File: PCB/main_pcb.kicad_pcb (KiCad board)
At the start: 2 copper layers, 116.9 x 116.9 mm, 40 parts, among them P1 SEN, P2 SRV, P3 PWR, P4 LED, P5 M1, P6 M2, P7 CONN_02X03, P8 CONN_02X03, P9 Range, Q1 5LN01SP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

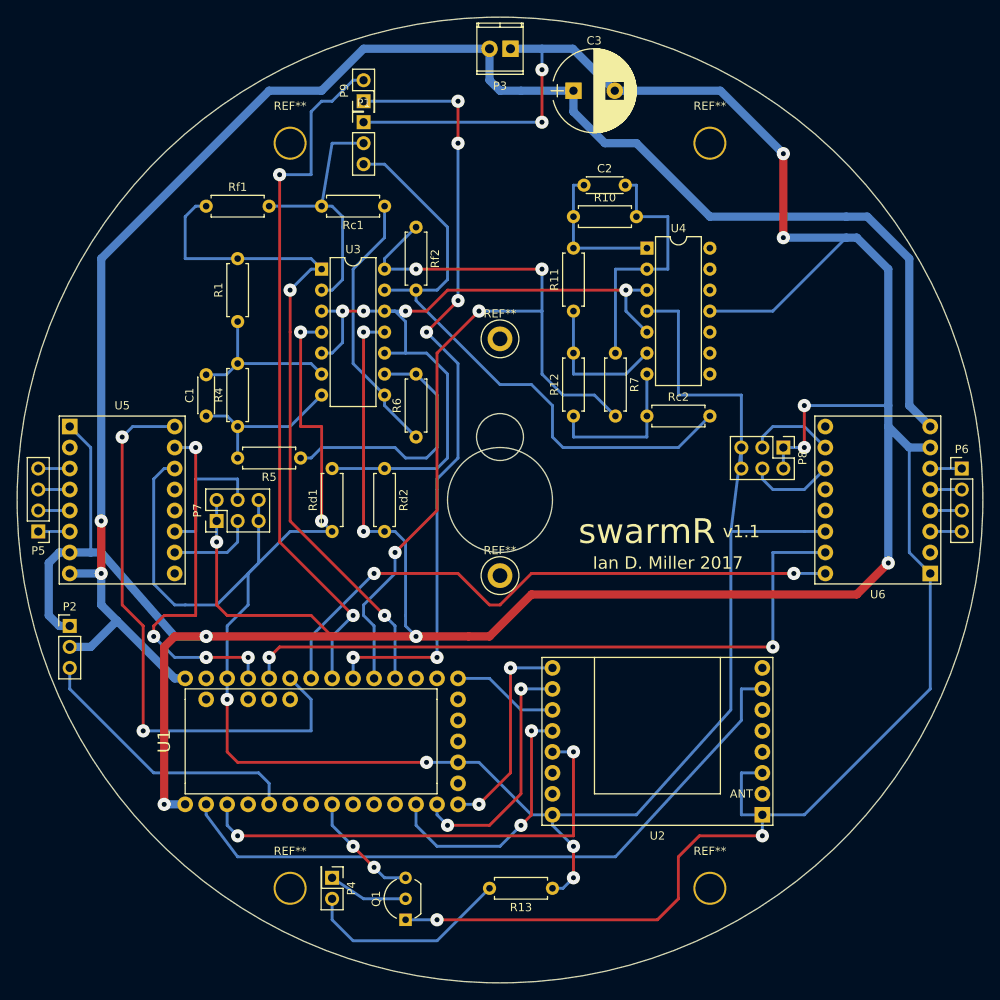
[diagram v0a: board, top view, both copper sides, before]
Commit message: Added copper pours
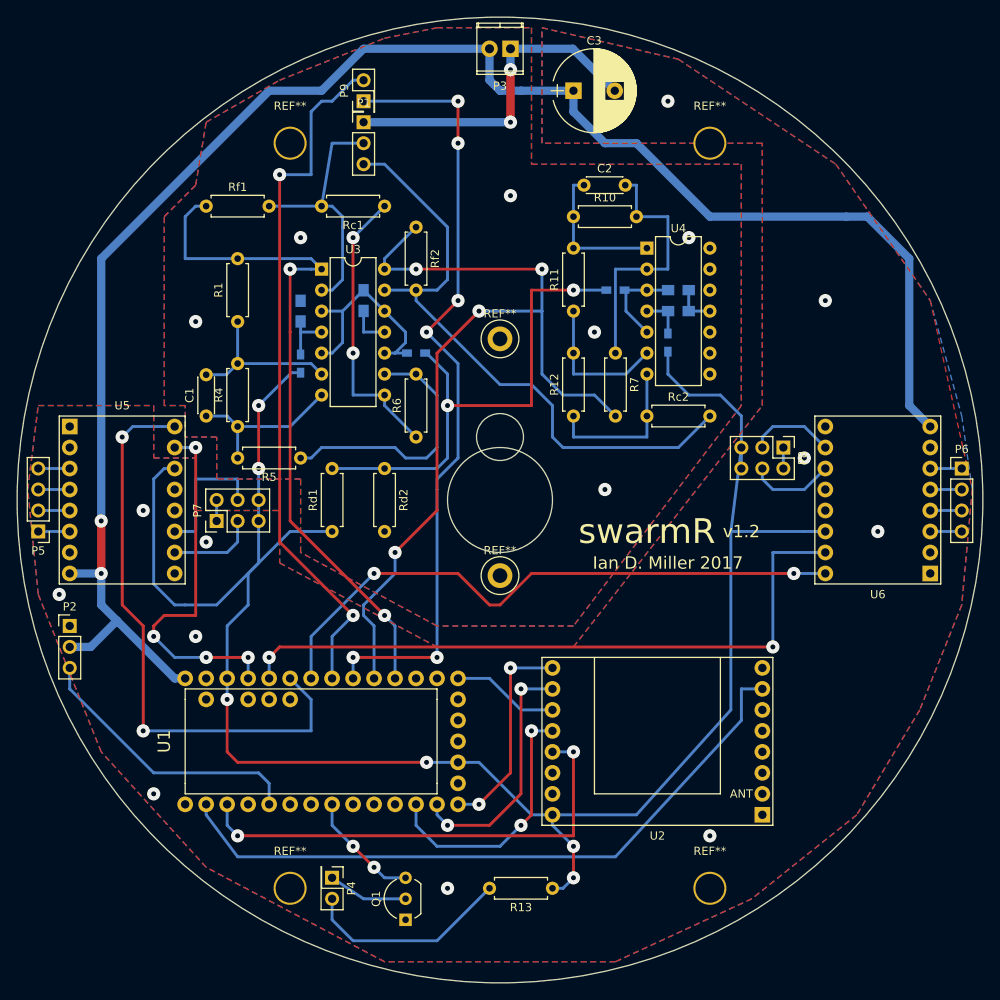
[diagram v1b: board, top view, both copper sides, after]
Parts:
- added C4: 10u, Capacitors_SMD:C_0805_HandSoldering, B.Cu at (114.3, 72.4)
- added C5: 10u, Capacitors_SMD:C_0805_HandSoldering, B.Cu at (121.9, 71.1)
- added C6: 10u, Capacitors_SMD:C_0805_HandSoldering, B.Cu at (160.0, 72.4)
- added C7: 10u, Capacitors_SMD:C_0805_HandSoldering, B.Cu at (160.0, 69.8)
- added R2: 500, Resistors_SMD:R_0603_HandSoldering, B.Cu at (114.3, 78.7)
- added R3: 10k, Resistors_SMD:R_0603_HandSoldering, B.Cu at (128.3, 77.5)
- added R8: 500, Resistors_SMD:R_0603_HandSoldering, B.Cu at (158.8, 76.2)
- added R9: 10k, Resistors_SMD:R_0603_HandSoldering, B.Cu at (152.4, 69.8)
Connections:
- U3 pad 10: /AnalogFilter1/Vref -> ref_filter
- U3 pad 12: /AnalogFilter1/Vref -> ref_filter
- U3 pad 3: /AnalogFilter1/Vref -> ref_filter
- U3 pad 4: +3V3 -> /AnalogFilter1/3v3f
- U3 pad 5: /AnalogFilter1/Vref -> ref_filter
- U4 pad 3: /AnalogFilter1/Vref -> ref_filter
- U4 pad 4: +3V3 -> /AnalogFilter2/3v3f
- U4 pad 5: /AnalogFilter1/Vref -> ref_filter
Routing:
- net GND: track 531.2 -> 56.7 mm, vias 15 -> 19
- net ref_filter: track 0.00 -> 37.2 mm
- net /AnalogFilter1/Vref: track 93.6 -> 61.6 mm, vias 4 -> 2
- net +3V3: track 259.1 -> 237.1 mm
- net /AnalogFilter1/3v3f: track 0.00 -> 6.54 mm
- net /AnalogFilter2/3v3f: track 0.00 -> 5.28 mm
- net Net-(R6-Pad1): track 32.7 -> 34.9 mm, vias 0 -> 2
- net /AnalogFilter1/Out: track 82.3 -> 83.8 mm
- added copper zone on B.Cu, net GND
- added copper zone on F.Cu, net GND
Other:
- board text added: "v1.2"
- board text removed: "v1.1"

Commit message: pcb tweaks
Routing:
- net GND: track 56.7 -> 220.1 mm, vias 19 -> 13
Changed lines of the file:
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@@
     (links 115)
     (no_connects 1)
-    (area 79.921196 36.741196 196.938804 153.758804)
+    (area 79.921196 35.01412 215.01 165.260001)
     (thickness 1.6)
     (drawings 11)
-    (tracks 402)
+    (tracks 422)
     (zones 0)
     (modules 48)
@@
   (segment (start 137.16 40.64) (end 121.92 40.64) (width 1) (layer B.Cu) (net 5))
   (segment (start 137.16 40.64) (end 137.16 44.45) (width 1) (layer B.Cu) (net 5))
-  (via (at 161.29 63.5) (size 1.6) (drill 0.6) (layers F.Cu B.Cu) (net 6))
-  (via (at 101.6 73.66) (size 1.6) (drill 0.6) (layers F.Cu B.Cu) (net 6))
-  (via (at 114.3 63.5) (size 1.6) (drill 0.6) (layers F.Cu B.Cu) (net 6))
-  (via (at 139.7 58.42) (size 1.6) (drill 0.6) (layers F.Cu B.Cu) (net 6))
-  (via (at 149.86 74.93) (size 1.6) (drill 0.6) (layers F.Cu B.Cu) (net 6))
-  (via (at 151.13 93.98) (size 1.6) (drill 0.6) (layers F.Cu B.Cu) (net 6))
-  (via (at 85.09 106.68) (size 1.6) (drill 0.6) (layers F.Cu B.Cu) (net 6))
+  (segment (start 124.46 74.93) (end 125.73 74.93) (width 0.35) (layer F.Cu) (net 6))
+  (segment (start 125.73 74.93) (end 130.81 69.85) (width 0.35) (layer F.Cu) (net 6))
+  (segment (start 121.92 49.53) (end 128.27 49.53) (width 0.35) (layer B.Cu) (net 6))
+  (via (at 128.27 49.53) (size 1.6) (drill 0.6) (layers F.Cu B.Cu) (net 6))
+  (segment (start 163.83 72.39) (end 166.37 72.39) (width 0.35) (layer F.Cu) (net 6))
+  (via (at 151.13 92.71) (size 1.6) (drill 0.6) (layers F.Cu B.Cu) (net 6))
+  (segment (start 158.75 92.71) (end 151.13 92.71) (width 0.35) (layer F.Cu) (net 6))
+  (segment (start 166.37 85.09) (end 158.75 92.71) (width 0.35) (layer F.Cu) (net 6))
+  (segment (start 166.37 72.39) (end 166.37 85.09) (width 0.35) (layer F.Cu) (net 6))
+  (segment (start 161.27 69.85) (end 161.27 62.25) (width 0.35) (layer B.Cu) (net 6))
+  (via (at 161.29 62.23) (size 1.6) (drill 0.6) (layers F.Cu B.Cu) (net 6))
+  (segment (start 161.27 62.25) (end 161.29 62.23) (width 0.35) (layer B.Cu) (net 6))
+  (segment (start 104.14 97.79) (end 104.14 99.06) (width 0.35) (layer F.Cu) (net 6))
+  (via (at 102.87 100.33) (size 1.6) (drill 0.6) (layers F.Cu B.Cu) (net 6))
+  (segment (start 104.14 99.06) (end 102.87 100.33) (width 0.35) (layer F.Cu) (net 6))
+  (segment (start 86.36 101.6) (end 90.17 101.6) (width 0.35) (layer B.Cu) (net 6))
   (via (at 95.25 96.52) (size 1.6) (drill 0.6) (layers F.Cu B.Cu) (net 6))
-  (via (at 101.6 111.76) (size 1.6) (drill 0.6) (layers F.Cu B.Cu) (net 6))
-  (via (at 102.87 100.33) (size 1.6) (drill 0.6) (layers F.Cu B.Cu) (net 6))
-  (via (at 96.52 130.81) (size 1.6) (drill 0.6) (layers F.Cu B.Cu) (net 6))
-  (via (at 132.08 142.24) (size 1.6) (drill 0.6) (layers F.Cu B.Cu) (net 6))
-  (via (at 163.83 135.89) (size 1.6) (drill 0.6) (layers F.Cu B.Cu) (net 6))
-  (via (at 184.15 99.06) (size 1.6) (drill 0.6) (layers F.Cu B.Cu) (net 6))
-  (via (at 158.75 46.99) (size 1.6) (drill 0.6) (layers F.Cu B.Cu) (net 6))
-  (via (at 177.8 71.12) (size 1.6) (drill 0.6) (layers F.Cu B.Cu) (net 6))
-  (via (at 175.26 90.17) (size 1.6) (drill 0.6) (layers F.Cu B.Cu) (net 6))
+  (segment (start 90.17 101.6) (end 95.25 96.52) (width 0.35) (layer B.Cu) (net 6))
+  (segment (start 127 146.05) (end 128.27 146.05) (width 0.35) (layer F.Cu) (net 6))
+  (via (at 133.35 140.97) (size 1.6) (drill 0.6) (layers F.Cu B.Cu) (net 6))
+  (segment (start 128.27 146.05) (end 133.35 140.97) (width 0.35) (layer F.Cu) (net 6))
+  (segment (start 170.18 133.35) (end 165.1 133.35) (width 0.35) (layer F.Cu) (net 6))
+  (via (at 153.67 144.78) (size 1.6) (drill 0.6) (layers F.Cu B.Cu) (net 6))
+  (segment (start 165.1 133.35) (end 153.67 144.78) (width 0.35) (layer F.Cu) (net 6))
+  (segment (start 190.5 88.9) (end 187.96 88.9) (width 0.35) (layer B.Cu) (net 6))
+  (via (at 177.8 67.31) (size 1.6) (drill 0.6) (layers F.Cu B.Cu) (net 6))
+  (segment (start 177.8 78.74) (end 177.8 67.31) (width 0.35) (layer B.Cu) (net 6))
+  (segment (start 187.96 88.9) (end 177.8 78.74) (width 0.35) (layer B.Cu) (net 6))
+  (segment (start 190.5 104.14) (end 190.5 109.22) (width 0.35) (layer F.Cu) (net 6))
+  (via (at 180.34 119.38) (size 1.6) (drill 0.6) (layers F.Cu B.Cu) (net 6))
+  (segment (start 190.5 109.22) (end 180.34 119.38) (width 0.35) (layer F.Cu) (net 6))
+  (segment (start 172.72 88.9) (end 175.26 88.9) (width 0.35) (layer B.Cu) (net 6))
+  (via (at 175.26 88.9) (size 1.6) (drill 0.6) (layers F.Cu B.Cu) (net 6))
+  (segment (start 124.46 74.93) (end 123.19 74.93) (width 0.35) (layer F.Cu) (net 6))
+  (via (at 121.92 86.36) (size 1.6) (drill 0.6) (layers F.Cu B.Cu) (net 6))
+  (segment (start 121.92 76.2) (end 121.92 86.36) (width 0.35) (layer F.Cu) (net 6))
+  (segment (start 123.19 74.93) (end 121.92 76.2) (width 0.35) (layer F.Cu) (net 6))
   (segment (start 139.7 40.64) (end 139.7 43.18) (width 1) (layer B.Cu) (net 6))
   (segment (start 139.7 49.53) (end 121.92 49.53) (width 1) (layer B.Cu) (net 6))
@@
   (segment (start 115.57 90.17) (end 116.84 88.9) (width 0.35) (layer B.Cu) (net 22))
   (segment (start 124.46 80.01) (end 128.27 80.01) (width 0.35) (layer B.Cu) (net 22))
-  (segment (start 124.46 82.55) (end 120.65 82.55) (width 0.35) (layer B.Cu) (net 23) (status 400000))
-  (segment (start 120.65 63.5) (end 124.46 59.69) (width 0.35) (layer B.Cu) (net 23) (status 800000))
+  (segment (start 124.46 82.55) (end 120.65 82.55) (width 0.35) (layer B.Cu) (net 23))
+  (segment (start 120.65 63.5) (end 124.46 59.69) (width 0.35) (layer B.Cu) (net 23))
   (via (at 120.65 63.5) (size 1.6) (drill 0.6) (layers F.Cu B.Cu) (net 23))
   (segment (start 120.65 77.47) (end 120.65 63.5) (width 0.35) (layer F.Cu) (net 23))

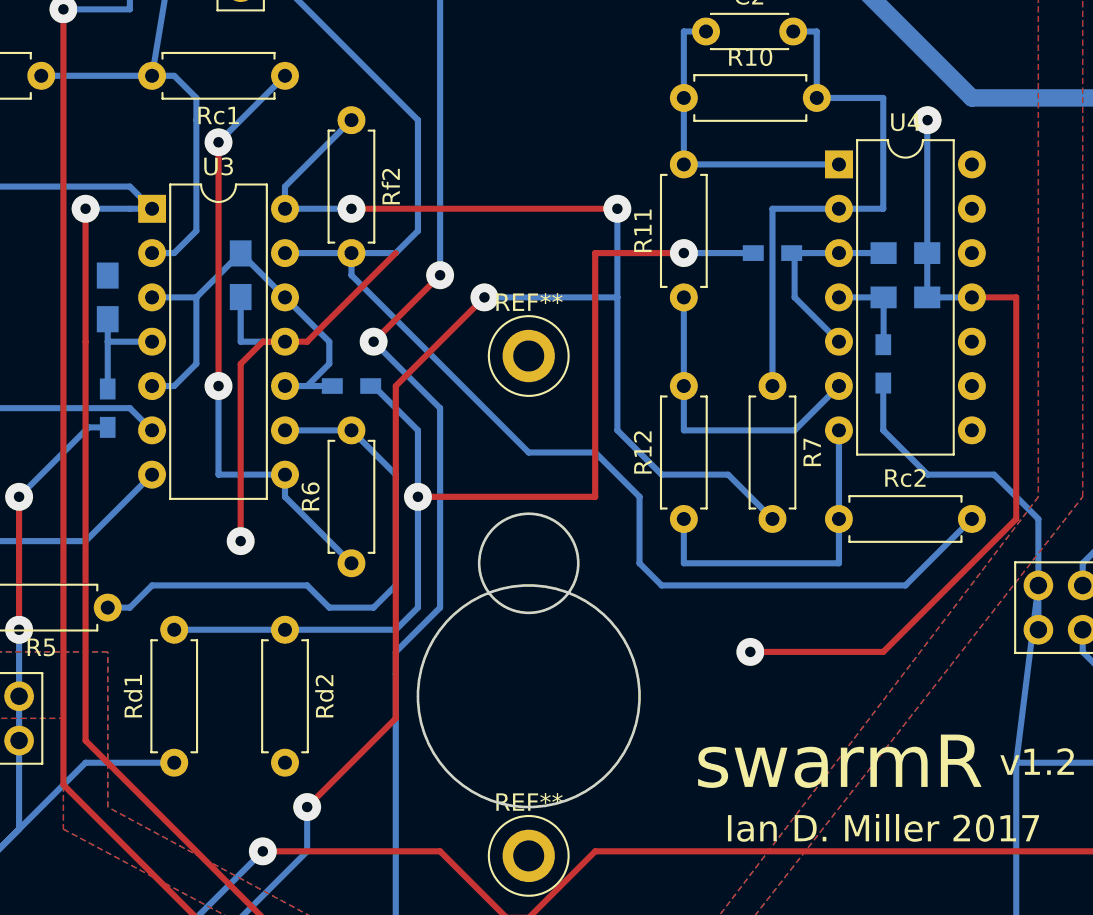
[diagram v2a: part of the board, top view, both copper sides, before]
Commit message: Fixed some motor speed modelling errors
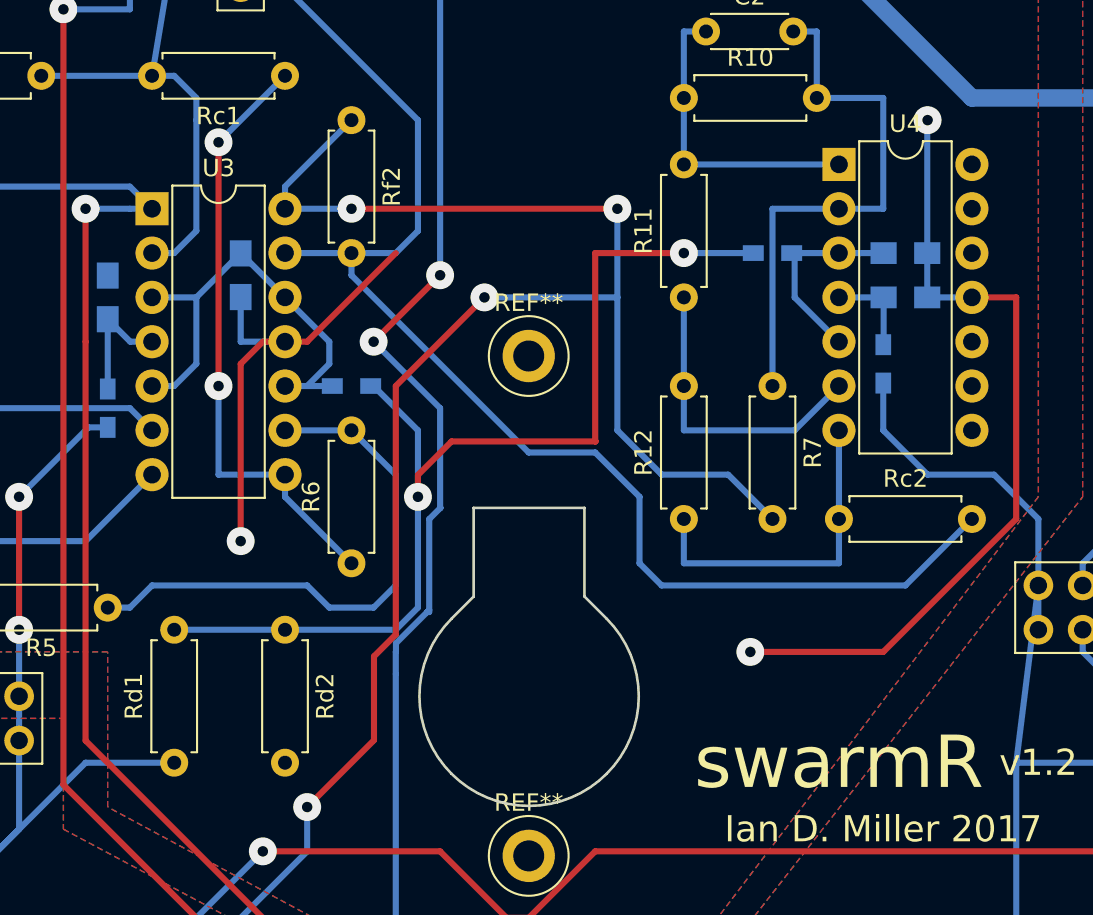
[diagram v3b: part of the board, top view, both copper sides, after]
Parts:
- U3, U4: footprint Housings_DIP:DIP-14_W7.62mm -> custom_footprints:DIP-14_W7.62mm_Socket
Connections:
- net /AnalogFilter1/Out renamed /FFT1
- net /AnalogFilter1/Sen renamed /Sen1
- net /AnalogFilter1/Vref renamed /Vref
- net /AnalogFilter2/Out renamed /FFT2
- net /AnalogFilter2/Sen renamed /Sen2
- C4 pad 2: /AnalogFilter1/3v3f -> 3v3f
- C6 pad 2: /AnalogFilter2/3v3f -> 3v3f
- R2 pad 1: /AnalogFilter1/3v3f -> 3v3f
- R8 pad 1: /AnalogFilter2/3v3f -> 3v3f
- U3 pad 4: /AnalogFilter1/3v3f -> 3v3f
- U4 pad 4: /AnalogFilter2/3v3f -> 3v3f
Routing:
- net 3v3f: track 0.00 -> 12.4 mm
- net /AnalogFilter1/3v3f: track 6.54 -> 0.00 mm
- net /AnalogFilter2/3v3f: track 5.28 -> 0.00 mm
- net /Vref: track 61.6 -> 60.5 mm
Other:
- outline, holes or cut-outs redrawn
- net class Production added: clearance 0.2, trace_width 0.35, via_dia 0.5, via_drill 0.3
